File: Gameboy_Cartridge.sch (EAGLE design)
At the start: 4 parts, among them IC1 AT49F040J

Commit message: Files sent to manufacture
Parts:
- added C1: 20nF, resistor:C-EUC0805
- R1: value 47000 -> 47K
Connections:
- new net 31: IC1.!WE, R1.1, U$1.VIN
- net A: now also IC1.A18, U$2.M18; no longer IC1.A16, U$2.M16
- net B: now also IC1.A17, U$2.M17; no longer IC1.A15, U$2.M15
- net C: now also IC1.A16, U$2.M16; no longer IC1.!WE, R1.1, U$1.VIN, U$2.M18
- net D: now also IC1.A15, U$2.M15; no longer IC1.A17, U$2.M17
- net GND: now also C1.2; no longer IC1.A18
- net VDD: now also C1.1

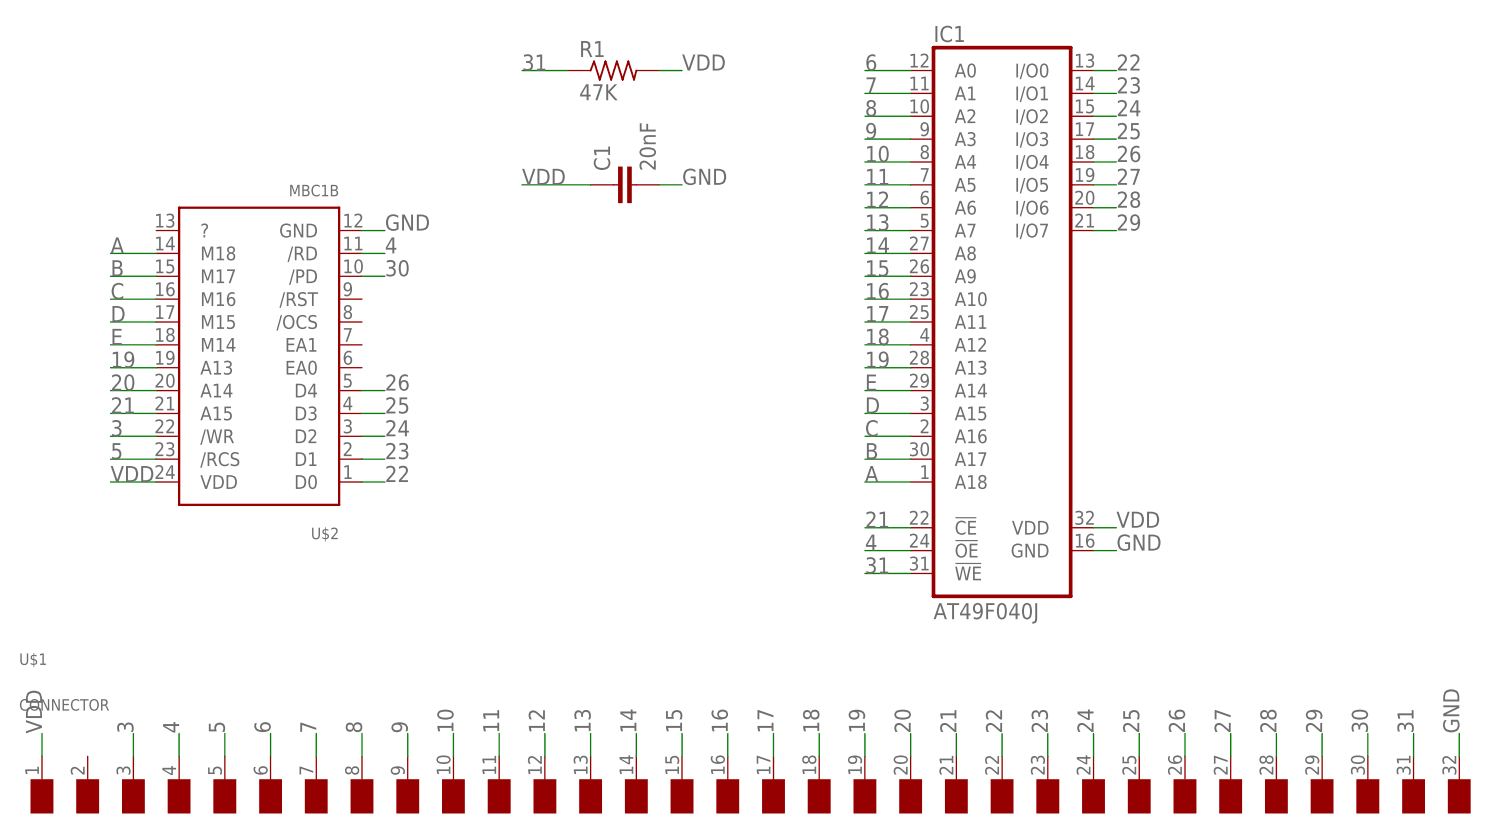
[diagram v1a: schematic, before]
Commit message: add solder jumpers where traces should be shorted for ROM only operation
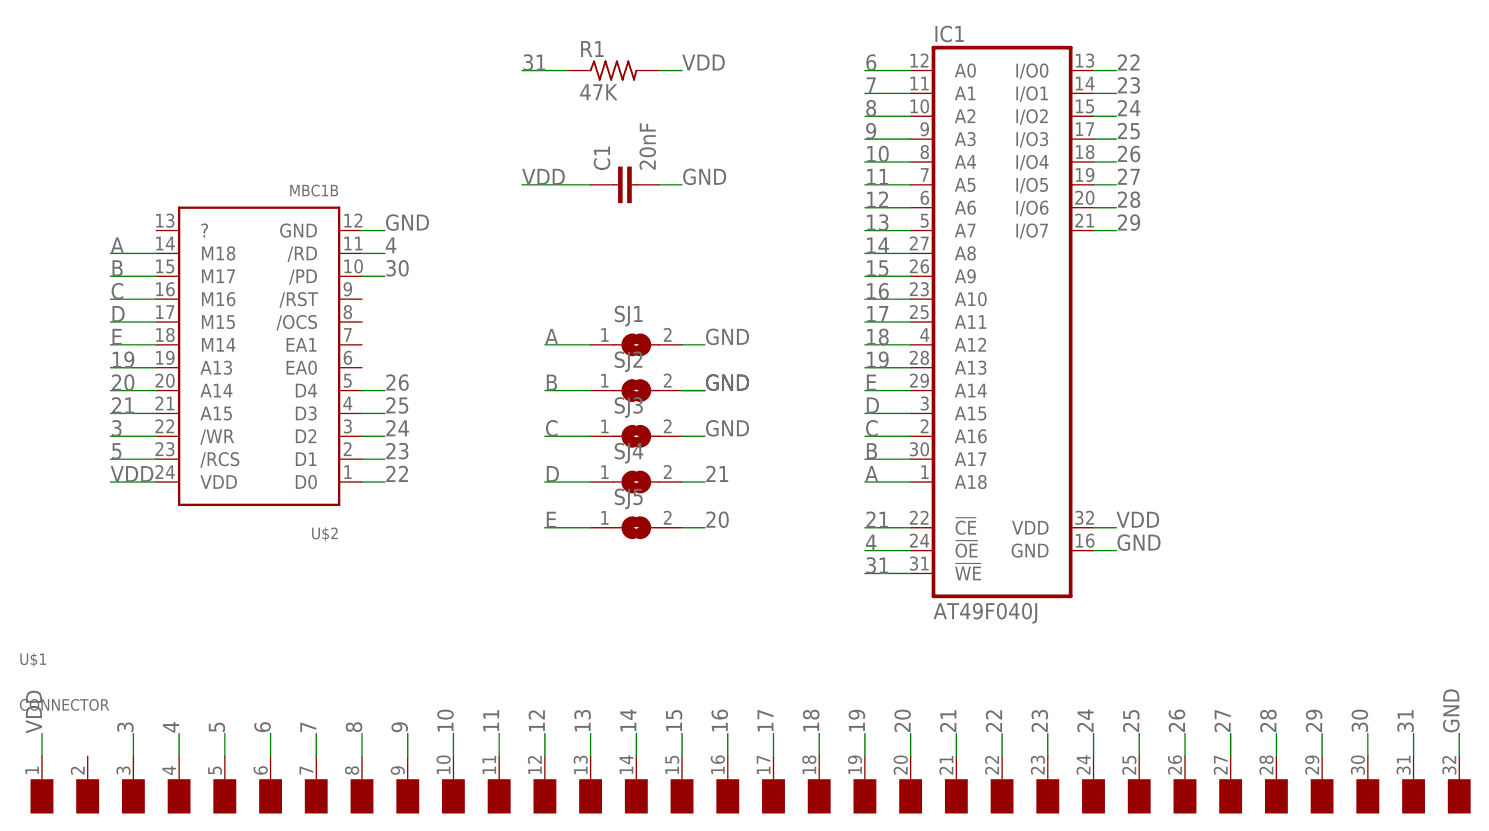
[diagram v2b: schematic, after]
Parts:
- added SJ1, SJ2, SJ3, SJ4, SJ5: (no value), jumper:SJ
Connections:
- net A: now also SJ1.1
- net B: now also SJ2.1, SJ3.1, SJ4.1
- net GND: now also SJ1.2, SJ2.2, SJ3.2, SJ4.2
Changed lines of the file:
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@@
 <?xml version="1.0" encoding="utf-8"?>
 <!DOCTYPE eagle SYSTEM "eagle.dtd">
-<eagle version="6.1">
+<eagle version="9.3.2">
 <drawing>
 <settings>
 <setting alwaysvectorfont="no"/>
+<setting keepoldvectorfont="yes"/>
 <setting verticaltext="up"/>
 </settings>
@@
 <part name="IC1" library="gameboy" deviceset="AT49F040J" device=""/>
 <part name="C1" library="resistor" deviceset="C-EU" device="C0805" value="20nF"/>
+<part name="SJ1" library="jumper" library_urn="urn:adsk.eagle:library:252" deviceset="SJ" device="" package3d_urn="urn:adsk.eagle:package:15471/1"/>
+<part name="SJ2" library="jumper" library_urn="urn:adsk.eagle:library:252" deviceset="SJ" device="" package3d_urn="urn:adsk.eagle:package:15471/1"/>
+<part name="SJ3" library="jumper" library_urn="urn:adsk.eagle:library:252" deviceset="SJ" device="" package3d_urn="urn:adsk.eagle:package:15471/1"/>
+<part name="SJ4" library="jumper" library_urn="urn:adsk.eagle:library:252" deviceset="SJ" device="" package3d_urn="urn:adsk.eagle:package:15471/1"/>
+<part name="SJ5" library="jumper" library_urn="urn:adsk.eagle:library:252" deviceset="SJ" device="" package3d_urn="urn:adsk.eagle:package:15471/1"/>
 </parts>
 <sheets>
@@
 </plain>
 <instances>
-<instance part="U$2" gate="G$1" x="25.4" y="81.28" rot="R180"/>
-<instance part="U$1" gate="G$1" x="-10.16" y="50.8"/>
-<instance part="R1" gate="G$1" x="55.88" y="129.54"/>
-<instance part="IC1" gate="G$1" x="99.06" y="101.6"/>
-<instance part="C1" gate="G$1" x="55.88" y="116.84" rot="R90"/>
+<instance part="U$2" gate="G$1" x="25.4" y="81.28" smashed="yes" rot="R180">
+<attribute name="NAME" x="25.4" y="78.74" size="1.27" layer="95" rot="R180"/>
+<attribute name="VALUE" x="25.4" y="116.84" size="1.27" layer="96" rot="R180"/>
+</instance>
+<instance part="U$1" gate="G$1" x="-10.16" y="50.8" smashed="yes">
+<attribute name="NAME" x="-10.16" y="63.5" size="1.27" layer="95"/>
+<attribute name="VALUE" x="-10.16" y="58.42" size="1.27" layer="96"/>
+</instance>
+<instance part="R1" gate="G$1" x="55.88" y="129.54" smashed="yes">
+<attribute name="NAME" x="52.07" y="131.0386" size="1.778" layer="95"/>
+<attribute name="VALUE" x="52.07" y="126.238" size="1.778" layer="96"/>
+</instance>
+<instance part="IC1" gate="G$1" x="99.06" y="101.6" smashed="yes">
+<attribute name="NAME" x="91.44" y="132.715" size="1.778" layer="95"/>
+<attribute name="VALUE" x="91.44" y="68.58" size="1.778" layer="96"/>
+</instance>
+<instance part="C1" gate="G$1" x="55.88" y="116.84" smashed="yes" rot="R90">
+<attribute name="NAME" x="55.499" y="118.364" size="1.778" layer="95" rot="R90"/>
+<attribute name="VALUE" x="60.579" y="118.364" size="1.778" layer="96" rot="R90"/>
+</instance>
+<instance part="SJ1" gate="1" x="58.42" y="99.06" smashed="yes">
+<attribute name="NAME" x="55.88" y="101.6" size="1.778" layer="95"/>
+<attribute name="VALUE" x="55.88" y="95.25" size="1.778" layer="96"/>
+</instance>
+<instance part="SJ2" gate="1" x="58.42" y="93.98" smashed="yes">
+<attribute name="NAME" x="55.88" y="96.52" size="1.778" layer="95"/>
+<attribute name="VALUE" x="55.88" y="90.17" size="1.778" layer="96"/>
+</instance>
+<instance part="SJ3" gate="1" x="58.42" y="88.9" smashed="yes">
+<attribute name="NAME" x="55.88" y="91.44" size="1.778" layer="95"/>
+<attribute name="VALUE" x="55.88" y="85.09" size="1.778" layer="96"/>
+</instance>
+<instance part="SJ4" gate="1" x="58.42" y="83.82" smashed="yes">
+<attribute name="NAME" x="55.88" y="86.36" size="1.778" layer="95"/>
+<attribute name="VALUE" x="55.88" y="80.01" size="1.778" layer="96"/>
+</instance>
+<instance part="SJ5" gate="1" x="58.42" y="78.74" smashed="yes">
+<attribute name="NAME" x="55.88" y="81.28" size="1.778" layer="95"/>
+<attribute name="VALUE" x="55.88" y="74.93" size="1.778" layer="96"/>
+</instance>
 </instances>
 <busses>
@@
 <wire x1="0" y1="91.44" x2="5.08" y2="91.44" width="0.1524" layer="91"/>
 <label x="0" y="91.44" size="1.778" layer="95"/>
+<label x="66.04" y="83.82" size="1.778" layer="95"/>
 </segment>
 <segment>
@@
 <wire x1="5.08" y1="93.98" x2="0" y2="93.98" width="0.1524" layer="91"/>
 <label x="0" y="93.98" size="1.778" layer="95"/>
+<label x="66.04" y="78.74" size="1.778" layer="95"/>
 </segment>
 <segment>
@@
 <wire x1="5.08" y1="99.06" x2="0" y2="99.06" width="0.1524" layer="91"/>
 <label x="0" y="99.06" size="1.778" layer="95"/>
+<label x="48.26" y="78.74" size="1.778" layer="95"/>
 </segment>
 </net>
@@
 <wire x1="0" y1="101.6" x2="5.08" y2="101.6" width="0.1524" layer="91"/>
 <label x="0" y="101.6" size="1.778" layer="95"/>
+<label x="48.26" y="83.82" size="1.778" layer="95"/>
 </segment>
 </net>
@@
 <wire x1="5.08" y1="104.14" x2="0" y2="104.14" width="0.1524" layer="91"/>
 <label x="0" y="104.14" size="1.778" layer="95"/>
+<label x="48.26" y="88.9" size="1.778" layer="95"/>
 </segment>
 </net>
@@
 <wire x1="60.96" y1="116.84" x2="63.5" y2="116.84" width="0.1524" layer="91"/>
 <label x="63.5" y="116.84" size="1.778" layer="95"/>
+<label x="66.04" y="99.06" size="1.778" layer="95"/>
+<label x="66.04" y="93.98" size="1.778" layer="95"/>
+<label x="66.04" y="93.98" size="1.778" layer="95"/>
+<label x="66.04" y="88.9" size="1.778" layer="95"/>
+</segment>
+<segment>
+<wire x1="63.5" y1="99.06" x2="66.04" y2="99.06" width="0.1524" layer="91"/>
+<pinref part="SJ1" gate="1" pin="2"/>
+</segment>
+<segment>
+<wire x1="63.5" y1="93.98" x2="66.04" y2="93.98" width="0.1524" layer="91"/>
+<pinref part="SJ2" gate="1" pin="2"/>
+<wire x1="63.5" y1="93.98" x2="66.04" y2="93.98" width="0.1524" layer="91"/>
+</segment>
+<segment>
+<wire x1="63.5" y1="88.9" x2="66.04" y2="88.9" width="0.1524" layer="91"/>
+<pinref part="SJ3" gate="1" pin="2"/>
+</segment>
+<segment>
+<wire x1="63.5" y1="83.82" x2="66.04" y2="83.82" width="0.1524" layer="91"/>
+<pinref part="SJ4" gate="1" pin="2"/>
+</segment>
+<segment>
+<wire x1="63.5" y1="78.74" x2="66.04" y2="78.74" width="0.1524" layer="91"/>
 </segment>
 </net>
@@
 <wire x1="0" y1="106.68" x2="5.08" y2="106.68" width="0.1524" layer="91"/>
 <label x="0" y="106.68" size="1.778" layer="95"/>
+<label x="48.26" y="93.98" size="1.778" layer="95"/>
+</segment>
+<segment>
+<wire x1="48.26" y1="93.98" x2="53.34" y2="93.98" width="0.1524" layer="91"/>
+<pinref part="SJ2" gate="1" pin="1"/>
+</segment>
+<segment>
+<wire x1="48.26" y1="88.9" x2="53.34" y2="88.9" width="0.1524" layer="91"/>
+<pinref part="SJ3" gate="1" pin="1"/>
+</segment>
+<segment>
+<wire x1="48.26" y1="83.82" x2="53.34" y2="83.82" width="0.1524" layer="91"/>
+<pinref part="SJ4" gate="1" pin="1"/>
+</segment>
+<segment>
+<wire x1="48.26" y1="78.74" x2="53.34" y2="78.74" width="0.1524" layer="91"/>
 </segment>
 </net>
@@
 <wire x1="5.08" y1="109.22" x2="0" y2="109.22" width="0.1524" layer="91"/>
 <label x="0" y="109.22" size="1.778" layer="95"/>
+<label x="48.26" y="99.06" size="1.778" layer="95"/>
+</segment>
+<segment>
+<wire x1="53.34" y1="99.06" x2="48.26" y2="99.06" width="0.1524" layer="91"/>
+<pinref part="SJ1" gate="1" pin="1"/>
 </segment>
 </net>
@@
 </schematic>
 </drawing>
+<compatibility>
+<note version="8.2" severity="warning">
+Since Version 8.2, EAGLE supports online libraries. The ids
+of those online libraries will not be understood (or retained)
+with this version.
+</note>
+<note version="8.3" severity="warning">
+Since Version 8.3, EAGLE supports URNs for individual library
+assets (packages, symbols, and devices). The URNs of those assets
+will not be understood (or retained) with this version.
+</note>
+<note version="8.3" severity="warning">
+Since Version 8.3, EAGLE supports the association of 3D packages
+with devices in libraries, schematics, and board files. Those 3D
+packages will not be understood (or retained) with this version.
+</note>
+</compatibility>
 </eagle>

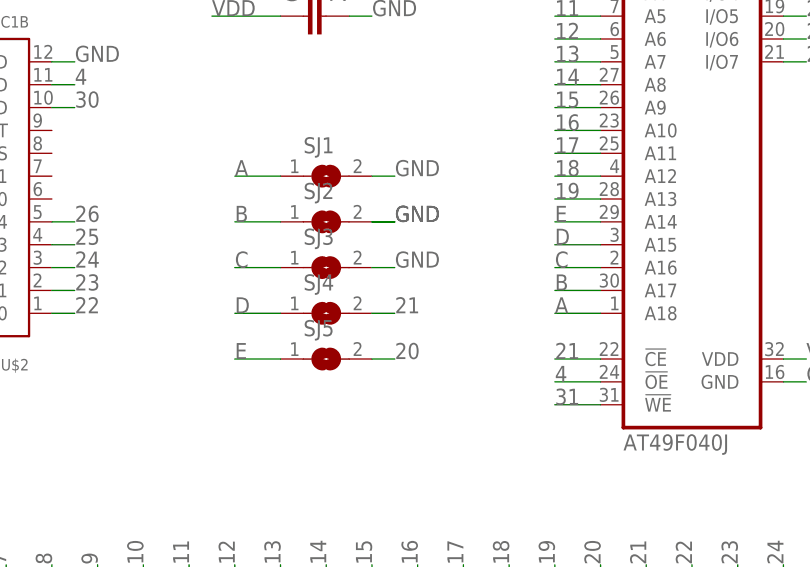
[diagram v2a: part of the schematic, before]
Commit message: replace the solder jumper with my new part
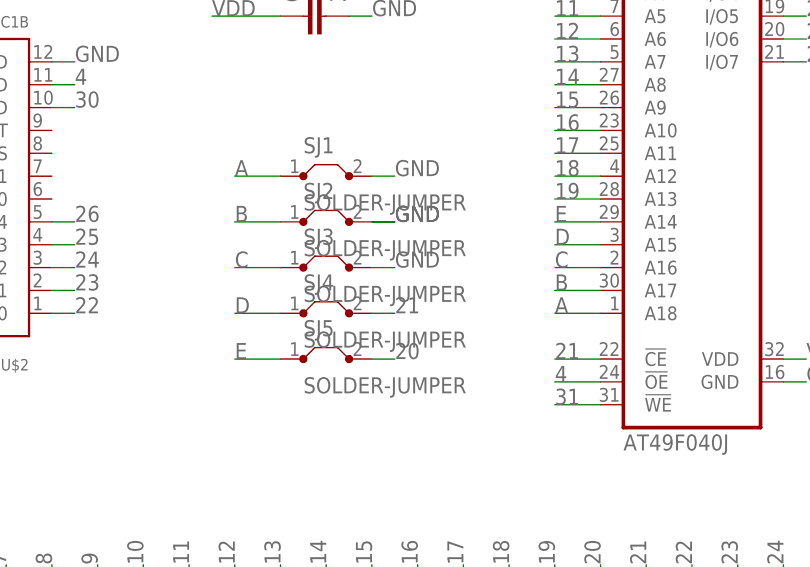
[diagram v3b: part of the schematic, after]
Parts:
- SJ1, SJ2, SJ3, SJ4, SJ5: value (none) -> SOLDER-JUMPER; device jumper:SJ -> gameboy:SOLDER-JUMPER
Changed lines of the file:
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@@
 <layer number="97" name="Info" color="7" fill="1" visible="yes" active="yes"/>
 <layer number="98" name="Guide" color="6" fill="1" visible="yes" active="yes"/>
+<layer number="99" name="SpiceOrder" color="5" fill="1" visible="yes" active="yes"/>
 </layers>
 <schematic xreflabel="%F%N/%S.%C%R" xrefpart="/%S.%C%R">
@@
 <part name="U$2" library="gameboy" deviceset="MBC1B" device=""/>
 <part name="U$1" library="gameboy" deviceset="CONNECTOR" device=""/>
-<part name="R1" library="resistor" deviceset="R-US_" device="M0805" value="47K"/>
+<part name="R1" library="resistor" library_urn="urn:adsk.eagle:library:348" deviceset="R-US_" device="M0805" package3d_urn="urn:adsk.eagle:package:23556/1" value="47K"/>
 <part name="IC1" library="gameboy" deviceset="AT49F040J" device=""/>
-<part name="C1" library="resistor" deviceset="C-EU" device="C0805" value="20nF"/>
-<part name="SJ1" library="jumper" library_urn="urn:adsk.eagle:library:252" deviceset="SJ" device="" package3d_urn="urn:adsk.eagle:package:15471/1"/>
-<part name="SJ2" library="jumper" library_urn="urn:adsk.eagle:library:252" deviceset="SJ" device="" package3d_urn="urn:adsk.eagle:package:15471/1"/>
-<part name="SJ3" library="jumper" library_urn="urn:adsk.eagle:library:252" deviceset="SJ" device="" package3d_urn="urn:adsk.eagle:package:15471/1"/>
-<part name="SJ4" library="jumper" library_urn="urn:adsk.eagle:library:252" deviceset="SJ" device="" package3d_urn="urn:adsk.eagle:package:15471/1"/>
-<part name="SJ5" library="jumper" library_urn="urn:adsk.eagle:library:252" deviceset="SJ" device="" package3d_urn="urn:adsk.eagle:package:15471/1"/>
+<part name="C1" library="resistor" library_urn="urn:adsk.eagle:library:348" deviceset="C-EU" device="C0805" package3d_urn="urn:adsk.eagle:package:23617/2" value="20nF"/>
+<part name="SJ1" library="gameboy" deviceset="SOLDER-JUMPER" device=""/>
+<part name="SJ2" library="gameboy" deviceset="SOLDER-JUMPER" device=""/>
+<part name="SJ3" library="gameboy" deviceset="SOLDER-JUMPER" device=""/>
+<part name="SJ4" library="gameboy" deviceset="SOLDER-JUMPER" device=""/>
+<part name="SJ5" library="gameboy" deviceset="SOLDER-JUMPER" device=""/>
 </parts>
 <sheets>
@@
 <attribute name="VALUE" x="60.579" y="118.364" size="1.778" layer="96" rot="R90"/>
 </instance>
-<instance part="SJ1" gate="1" x="58.42" y="99.06" smashed="yes">
+<instance part="SJ1" gate="G$1" x="58.42" y="99.06" smashed="yes">
 <attribute name="NAME" x="55.88" y="101.6" size="1.778" layer="95"/>
 <attribute name="VALUE" x="55.88" y="95.25" size="1.778" layer="96"/>
 </instance>
-<instance part="SJ2" gate="1" x="58.42" y="93.98" smashed="yes">
+<instance part="SJ2" gate="G$1" x="58.42" y="93.98" smashed="yes">
 <attribute name="NAME" x="55.88" y="96.52" size="1.778" layer="95"/>
 <attribute name="VALUE" x="55.88" y="90.17" size="1.778" layer="96"/>
 </instance>
-<instance part="SJ3" gate="1" x="58.42" y="88.9" smashed="yes">
+<instance part="SJ3" gate="G$1" x="58.42" y="88.9" smashed="yes">
 <attribute name="NAME" x="55.88" y="91.44" size="1.778" layer="95"/>
 <attribute name="VALUE" x="55.88" y="85.09" size="1.778" layer="96"/>
 </instance>
-<instance part="SJ4" gate="1" x="58.42" y="83.82" smashed="yes">
+<instance part="SJ4" gate="G$1" x="58.42" y="83.82" smashed="yes">
 <attribute name="NAME" x="55.88" y="86.36" size="1.778" layer="95"/>
 <attribute name="VALUE" x="55.88" y="80.01" size="1.778" layer="96"/>
 </instance>
-<instance part="SJ5" gate="1" x="58.42" y="78.74" smashed="yes">
+<instance part="SJ5" gate="G$1" x="58.42" y="78.74" smashed="yes">
 <attribute name="NAME" x="55.88" y="81.28" size="1.778" layer="95"/>
 <attribute name="VALUE" x="55.88" y="74.93" size="1.778" layer="96"/>
@@
 <segment>
 <wire x1="63.5" y1="99.06" x2="66.04" y2="99.06" width="0.1524" layer="91"/>
-<pinref part="SJ1" gate="1" pin="2"/>
+<pinref part="SJ1" gate="G$1" pin="2"/>
 </segment>
 <segment>
 <wire x1="63.5" y1="93.98" x2="66.04" y2="93.98" width="0.1524" layer="91"/>
-<pinref part="SJ2" gate="1" pin="2"/>
+<pinref part="SJ2" gate="G$1" pin="2"/>
 <wire x1="63.5" y1="93.98" x2="66.04" y2="93.98" width="0.1524" layer="91"/>
 </segment>
 <segment>
 <wire x1="63.5" y1="88.9" x2="66.04" y2="88.9" width="0.1524" layer="91"/>
-<pinref part="SJ3" gate="1" pin="2"/>
+<pinref part="SJ3" gate="G$1" pin="2"/>
 </segment>
 <segment>
 <wire x1="63.5" y1="83.82" x2="66.04" y2="83.82" width="0.1524" layer="91"/>
-<pinref part="SJ4" gate="1" pin="2"/>
+<pinref part="SJ4" gate="G$1" pin="2"/>
 </segment>
 <segment>
@@
 <segment>
 <wire x1="48.26" y1="93.98" x2="53.34" y2="93.98" width="0.1524" layer="91"/>
-<pinref part="SJ2" gate="1" pin="1"/>
+<pinref part="SJ2" gate="G$1" pin="1"/>
 </segment>
 <segment>
 <wire x1="48.26" y1="88.9" x2="53.34" y2="88.9" width="0.1524" layer="91"/>
-<pinref part="SJ3" gate="1" pin="1"/>
+<pinref part="SJ3" gate="G$1" pin="1"/>
 </segment>
 <segment>
 <wire x1="48.26" y1="83.82" x2="53.34" y2="83.82" width="0.1524" layer="91"/>
-<pinref part="SJ4" gate="1" pin="1"/>
+<pinref part="SJ4" gate="G$1" pin="1"/>
 </segment>
 <segment>
@@
 <segment>
 <wire x1="53.34" y1="99.06" x2="48.26" y2="99.06" width="0.1524" layer="91"/>
-<pinref part="SJ1" gate="1" pin="1"/>
-</segment>
-</net>
+<pinref part="SJ1" gate="G$1" pin="1"/>
+</segment>
+</net>
